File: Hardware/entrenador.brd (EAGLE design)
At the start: 121.9 x 70.8 mm, 63 parts, among them U1 DRV8833

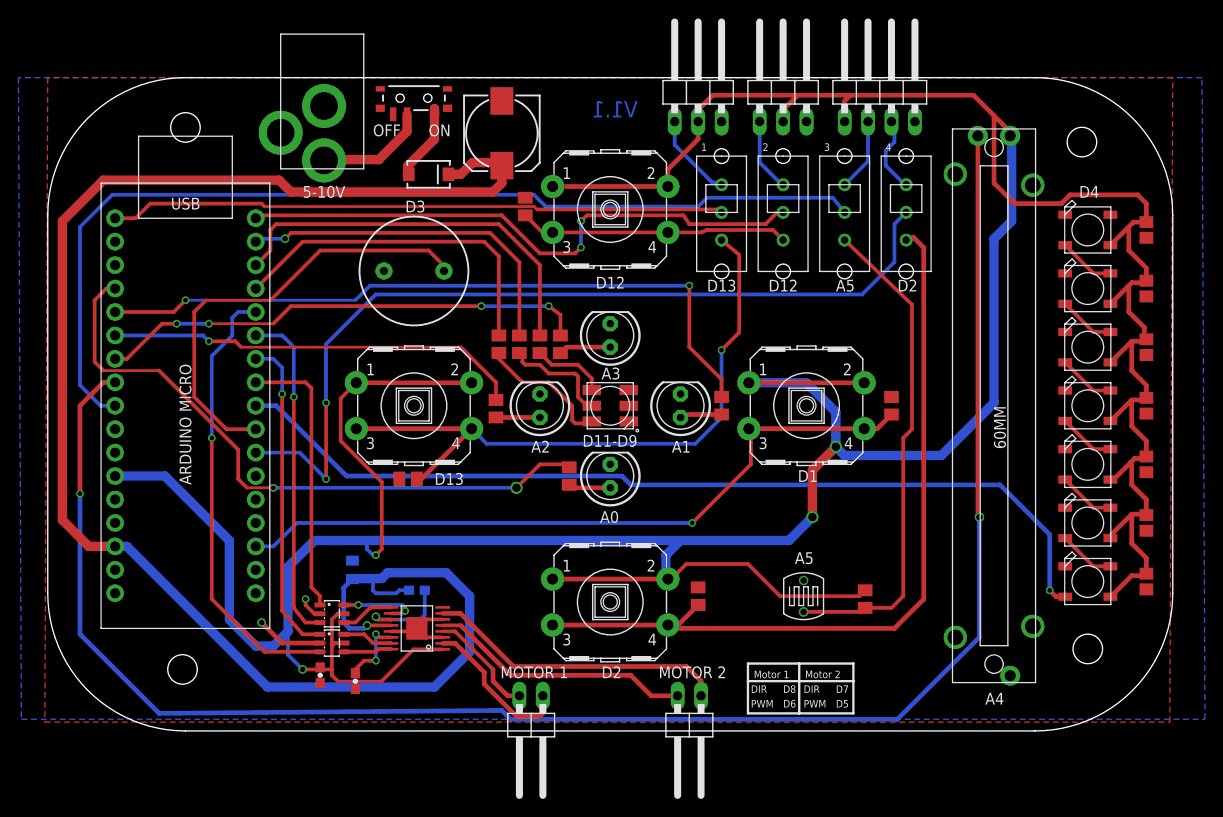
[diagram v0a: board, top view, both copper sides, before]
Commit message: FALTA PONER LA SERIGRAFIA  .Arreglados todos los issues del circuito salvo determinar por que los pines meten ruido.
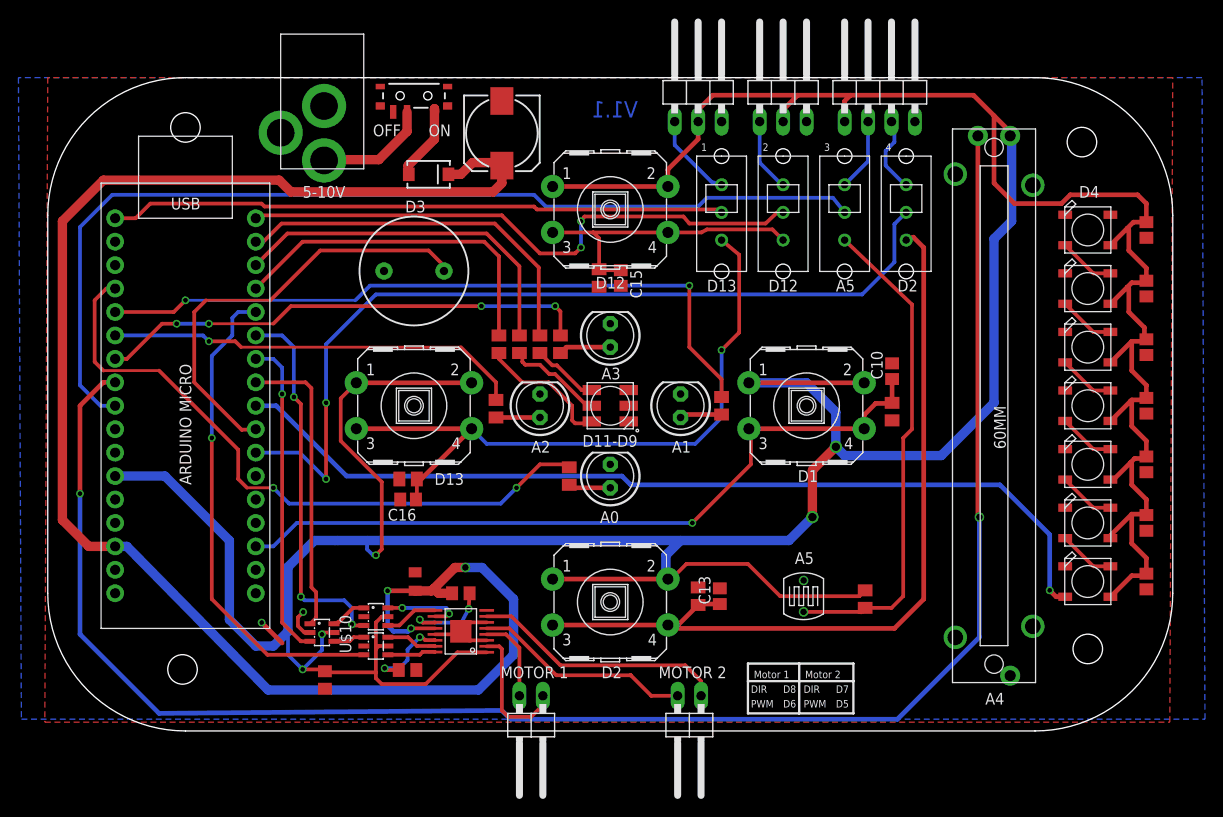
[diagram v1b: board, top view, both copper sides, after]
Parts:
- added C10, C13, C15, C16: 100n, adafruit:C0805
- added U$10: SN74LVC2G04SOT23-6, frizzy:SOT23-6
- C11, C12, C9: device SparkFun-Passives:0603-CAP -> rcl:C0805
- moved R7 11.1 mm to (59.8, 55.4), turned to 90 degrees
- moved C14 6.91 mm to (39.8, 22.5), flipped to the top
- moved C11 5.78 mm to (39.0, 13.0), turned to 0 degrees
- moved U$1 4.77 mm to (35.6, 15.6)
- moved U$9 4.77 mm to (35.6, 18.7)
- moved C12 4.77 mm to (44.8, 21.3), flipped to the top, turned to 180 degrees
- moved U1 4.77 mm to (44.8, 17.1)
- moved C9 0.72 mm to (30.0, 11.9)
- moved R5 0.64 mm to (91.5, 41.0), turned to 90 degrees
- moved S5 0.25 mm to (39.7, 75.2)
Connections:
- new net PWMA_N: U$1.1, U$10.4
- new net PWMB_N: U$10.6, U$9.1
- net GND: now also C10.2, C13.2, C15.2, C16.2, U$10.2
- net PB1: now also C10.1
- net PB2: now also C13.1
- net PB3: now also C15.1
- net PB4: now also C16.1
- net PWMA: now also U$10.3; no longer U$1.1
- net PWMB: now also U$10.1; no longer U$9.1
- net RGB_G: now also R13.2; no longer R12.2
- net RGB_R: now also R12.2; no longer R13.2
- net VCC: now also U$10.5
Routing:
- net VCC: track 459.9 -> 470.7 mm, vias 4 -> 5
- net M2B: track 28.6 -> 23.7 mm
- net M2A: track 32.6 -> 27.7 mm
- net DIRA: track 48.3 -> 53.2 mm
- net DIRB: track 36.5 -> 41.2 mm, vias 1 -> 3
- net RGB_G: track 43.4 -> 39.0 mm
- net PB1: track 77.4 -> 81.4 mm
- net PWMB_N: track 0.00 -> 3.90 mm
- net PWMA_N: track 0.00 -> 3.43 mm
- net GND: track 19.2 -> 15.8 mm
- net PB3: track 29.2 -> 32.2 mm
- net RGB_R: track 38.2 -> 40.9 mm, vias 1 -> 0
- net M1B: track 11.9 -> 9.36 mm
- net VIN: track 181.1 -> 183.6 mm, vias 1 -> 3
- net PB2: track 86.4 -> 88.8 mm
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
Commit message: me falto revisar una cosa del anterior commit, disculpas. curregido
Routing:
- net GND: track 15.8 -> 18.3 mm
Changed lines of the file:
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@@
 <contactref element="C15" pad="2"/>
 <contactref element="C16" pad="2"/>
-<wire x1="34.26" y1="15.5575" x2="34.26" y2="18.7325" width="0" layer="19" extent="1-1"/>
-<wire x1="39.939" y1="12.954" x2="41.9675" y2="16.82" width="0" layer="19" extent="1-1"/>
+<wire x1="34.26" y1="18.7325" x2="35.052" y2="18.7325" width="0.4064" layer="1"/>
+<wire x1="35.052" y1="18.7325" x2="35.56" y2="19.2405" width="0.4064" layer="1"/>
+<wire x1="35.56" y1="19.2405" x2="35.56" y2="20.193" width="0.4064" layer="1"/>
 </signal>
 <signal name="VCC">
@@
 <contactref element="U1" pad="1"/>
 <contactref element="C9" pad="1"/>
-<wire x1="47.5675" y1="14.87" x2="44.3975" y2="14.87" width="0.4064" layer="1"/>
-<wire x1="44.3975" y1="14.87" x2="40.9575" y2="11.43" width="0.4064" layer="1"/>
-<wire x1="40.9575" y1="11.43" x2="36.195" y2="11.43" width="0.4064" layer="1"/>
+<wire x1="44.1275" y1="11.43" x2="36.195" y2="11.43" width="0.4064" layer="1"/>
 <wire x1="36.195" y1="11.43" x2="35.56" y2="12.065" width="0.4064" layer="1"/>
 <wire x1="35.56" y1="12.065" x2="35.56" y2="12.7" width="0.4064" layer="1"/>
@@
 <wire x1="29.718" y1="16.8275" x2="29.718" y2="15.113" width="0.4064" layer="16"/>
 <wire x1="29.718" y1="15.113" x2="27.6225" y2="13.0175" width="0.4064" layer="16"/>
+<wire x1="44.1275" y1="11.43" x2="47.5675" y2="14.87" width="0.4064" layer="1"/>
 </signal>
 <signal name="M1B">
@@
 <contactref element="U$8" pad="P$5"/>
 <contactref element="U$1" pad="3"/>
-<wire x1="23.81" y1="14.6075" x2="17.78" y2="20.6375" width="0.4064" layer="1"/>
 <wire x1="17.78" y1="20.6375" x2="17.78" y2="38.1" width="0.4064" layer="1"/>
 <via x="17.78" y="38.1" extent="1-16" drill="0.5"/>
@@
 <wire x1="20.0025" y1="51.1175" x2="20.6375" y2="51.7525" width="0.4064" layer="16"/>
 <wire x1="20.6375" y1="51.7525" x2="22.5425" y2="51.7525" width="0.4064" layer="16"/>
-<wire x1="34.26" y1="14.6075" x2="23.81" y2="14.6075" width="0.4064" layer="1"/>
+<wire x1="34.26" y1="14.6075" x2="32.07" y2="14.6075" width="0.4064" layer="1"/>
+<wire x1="32.07" y1="14.6075" x2="31.496" y2="14.0335" width="0.4064" layer="1"/>
+<wire x1="31.496" y1="14.0335" x2="24.384" y2="14.0335" width="0.4064" layer="1"/>
+<wire x1="24.384" y1="14.0335" x2="17.78" y2="20.6375" width="0.4064" layer="1"/>
 </signal>
 <signal name="VIN">

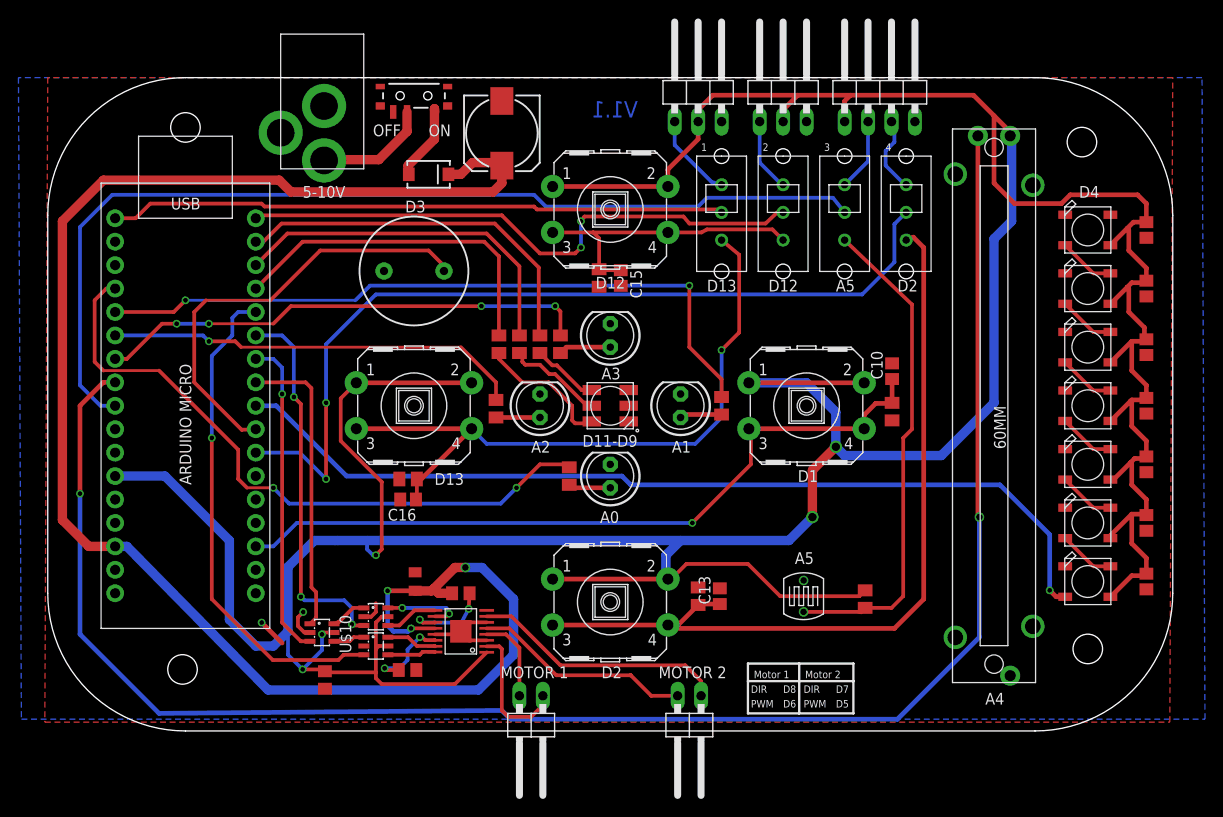
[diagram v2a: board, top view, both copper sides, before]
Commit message: Serigrafia TechTalents Añadida
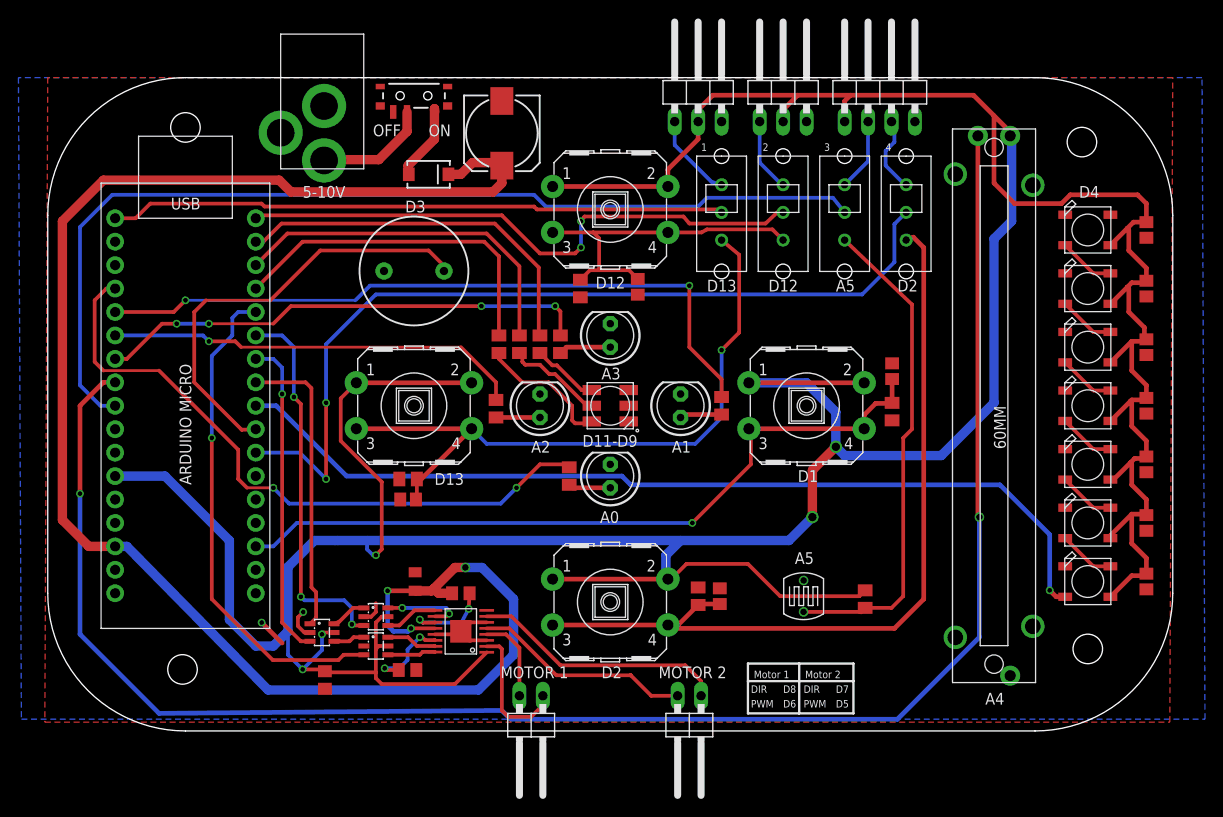
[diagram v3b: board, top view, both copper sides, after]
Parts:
- moved R7 2.33 mm to (57.7, 54.3)
- moved C15 2.07 mm to (63.9, 54.5)
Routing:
- net PB3: track 32.2 -> 37.0 mm
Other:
- board text added: "v1.1"
- board text removed: "V1.1"
- board text removed: "v1.0"

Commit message: Ultima version
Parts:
- moved C15 6.93 mm to (57.0, 54.2)
- moved R7 1.46 mm to (59.2, 54.2)
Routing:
- net PB3: track 37.0 -> 33.8 mm
